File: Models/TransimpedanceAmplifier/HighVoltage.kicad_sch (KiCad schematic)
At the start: 3 parts, among them U11 LM7815, 15V, 5%, U12 LM7915, -15V, 5%

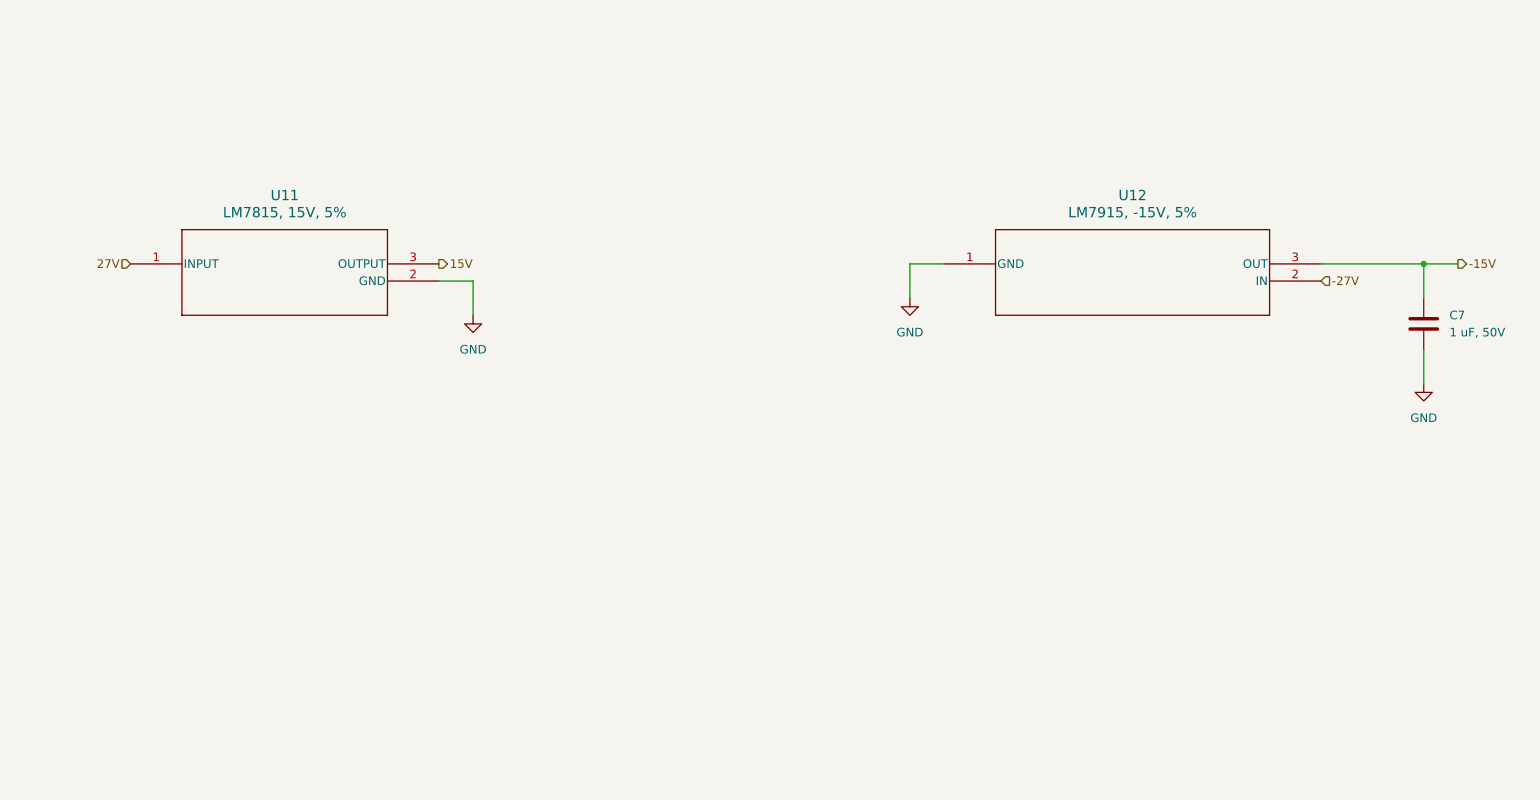
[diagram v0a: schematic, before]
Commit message: Finished the decoupling networks for the power subsystem
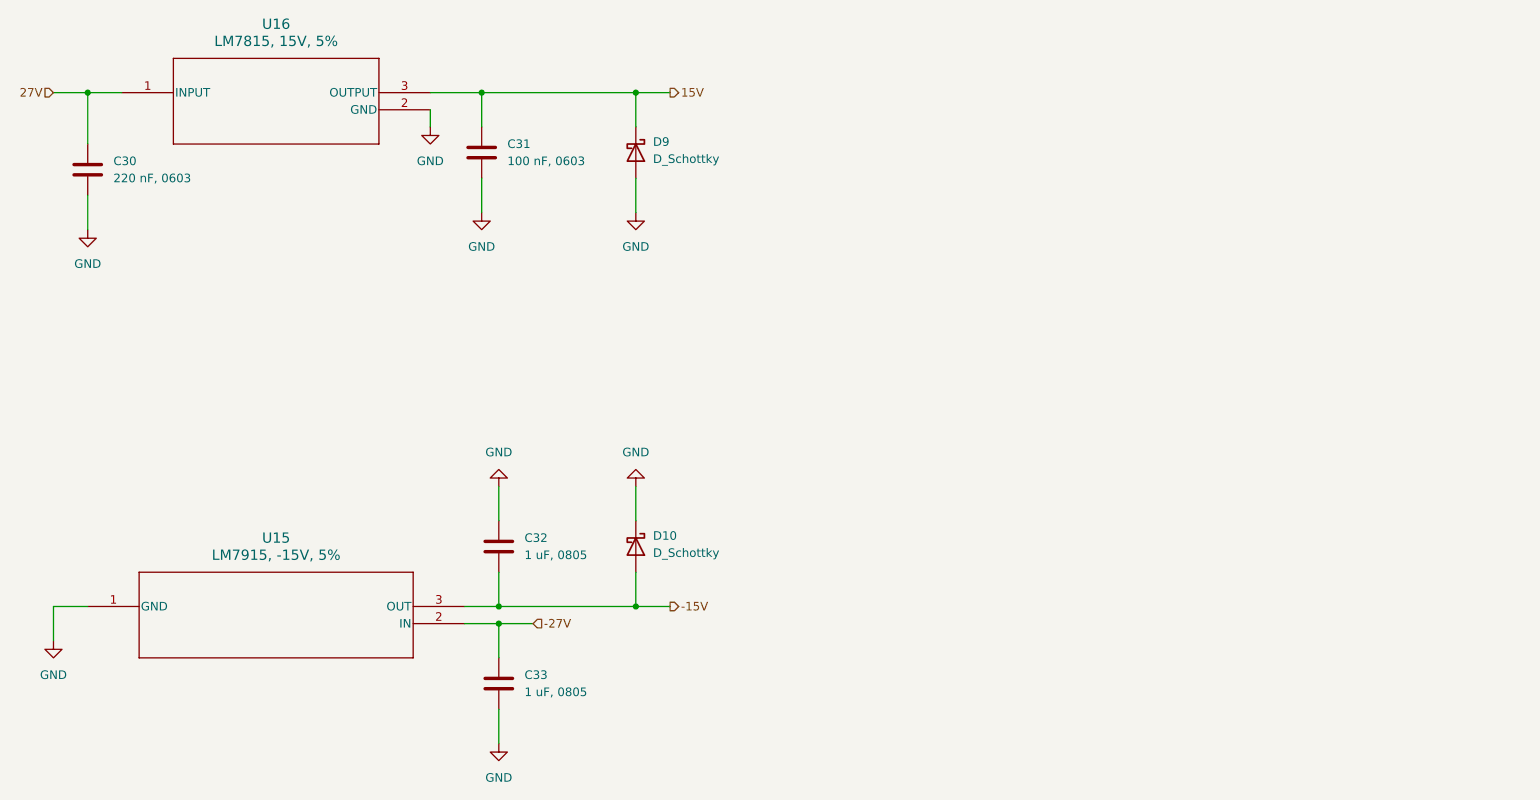
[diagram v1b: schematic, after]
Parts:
- removed C7: 1 uF, 50V, symbol Device:C
- removed U11: LM7815, 15V, 5%, NDE3_TEX, symbol LM78:LM7805CT_NOPB
- removed U12: LM7915, -15V, 5%, T03B_TEX, symbol LM79:LM7905CT
- added C30: 220 nF, 0603, symbol Device:C
- added C31: 100 nF, 0603, symbol Device:C
- added C32, C33: 1 uF, 0805, symbol Device:C
- added D10, D9: D_Schottky, symbol Device:D_Schottky
- added U15: LM7915, -15V, 5%, T03B_TEX, symbol LM79:LM7905CT
- added U16: LM7815, 15V, 5%, NDE3_TEX, symbol LM78:LM7805CT_NOPB
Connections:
- net -15V: now also C32.2, D10.2 (A), U15.3 (OUT)
- net -27V: now also C33.1, U15.2 (IN)
- net 15V: now also C31.1, D9.1 (K), U16.3 (OUTPUT)
- net 27V: now also C30.1, U16.1 (INPUT)
- net GND: now also C30.2, C31.2, C32.1, C33.2, D10.1 (K), D9.2 (A), U15.1 (GND), U16.2 (GND)

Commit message: Finished for today
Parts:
- C30, C31, C32, C33: Purchase Link (none) -> https://www.digikey.com/en/products/detail/murata-electroni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
- D10, D9: Purchase Link (none) -> https://www.digikey.com/en/products/detail/diodes-incorpora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
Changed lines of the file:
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@@
+			)
+		)
+		(property "Purchase Link" "https://www.digikey.com/en/products/detail/murata-electronics/GRM188R71H224KAC4D/5797498"
+			(at 53.34 67.31 0)
+			(effects
+				(font
+					(size 1.27 1.27)
+				)
+				(hide yes)
 			)
 		)
@@
 			)
 		)
+		(property "Purchase Link" "https://www.digikey.com/en/products/detail/murata-electronics/GRM188R72A104KA35D/702549"
+			(at 111.76 64.77 0)
+			(effects
+				(font
+					(size 1.27 1.27)
+				)
+				(hide yes)
+			)
+		)
 		(pin "1"
 		)
@@
 			)
 		)
+		(property "Purchase Link" "https://www.digikey.com/en/products/detail/diodes-incorporated/1N5819HW-7-F/814970"
+			(at 134.62 64.77 90)
+			(effects
+				(font
+					(size 1.27 1.27)
+				)
+				(hide yes)
+			)
+		)
 		(pin "1"
 		)
@@
 			)
 		)
+		(property "Purchase Link" "https://www.digikey.com/en/products/detail/murata-electronics/GRT21BR71H105KE01L/10702345"
+			(at 114.3 143.51 0)
+			(effects
+				(font
+					(size 1.27 1.27)
+				)
+				(hide yes)
+			)
+		)
 		(pin "1"
 		)
@@
 			)
 		)
+		(property "Purchase Link" "https://www.digikey.com/en/products/detail/diodes-incorporated/1N5819HW-7-F/814970"
+			(at 134.62 123.19 90)
+			(effects
+				(font
+					(size 1.27 1.27)
+				)
+				(hide yes)
+			)
+		)
 		(pin "1"
 		)
@@
 			(at 114.3 123.19 0)
 			(effects
+				(font
+					(size 1.27 1.27)
+				)
+				(hide yes)
+			)
+		)
+		(property "Purchase Link" "https://www.digikey.com/en/products/detail/murata-electronics/GRT21BR71H105KE01L/10702345"
+			(at 114.3 123.19 0)
+			(effects

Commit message: Save progress
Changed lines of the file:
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@@
 	)
 	(symbol
+		(lib_name "D_Schottky_1")
 		(lib_id "Device:D_Schottky")
 		(at 134.62 64.77 270)

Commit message: Save progress
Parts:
- U15: footprint T03B_TEX -> (none)
- U16: footprint NDE3_TEX -> (none)
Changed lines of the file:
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@@
 			)
 		)
-		(property "Footprint" "T03B_TEX"
+		(property "Footprint" ""
 			(at 53.34 132.08 0)
 			(effects
@@
 			)
 		)
-		(property "Footprint" "NDE3_TEX"
+		(property "Footprint" ""
 			(at 58.42 55.88 0)
 			(effects

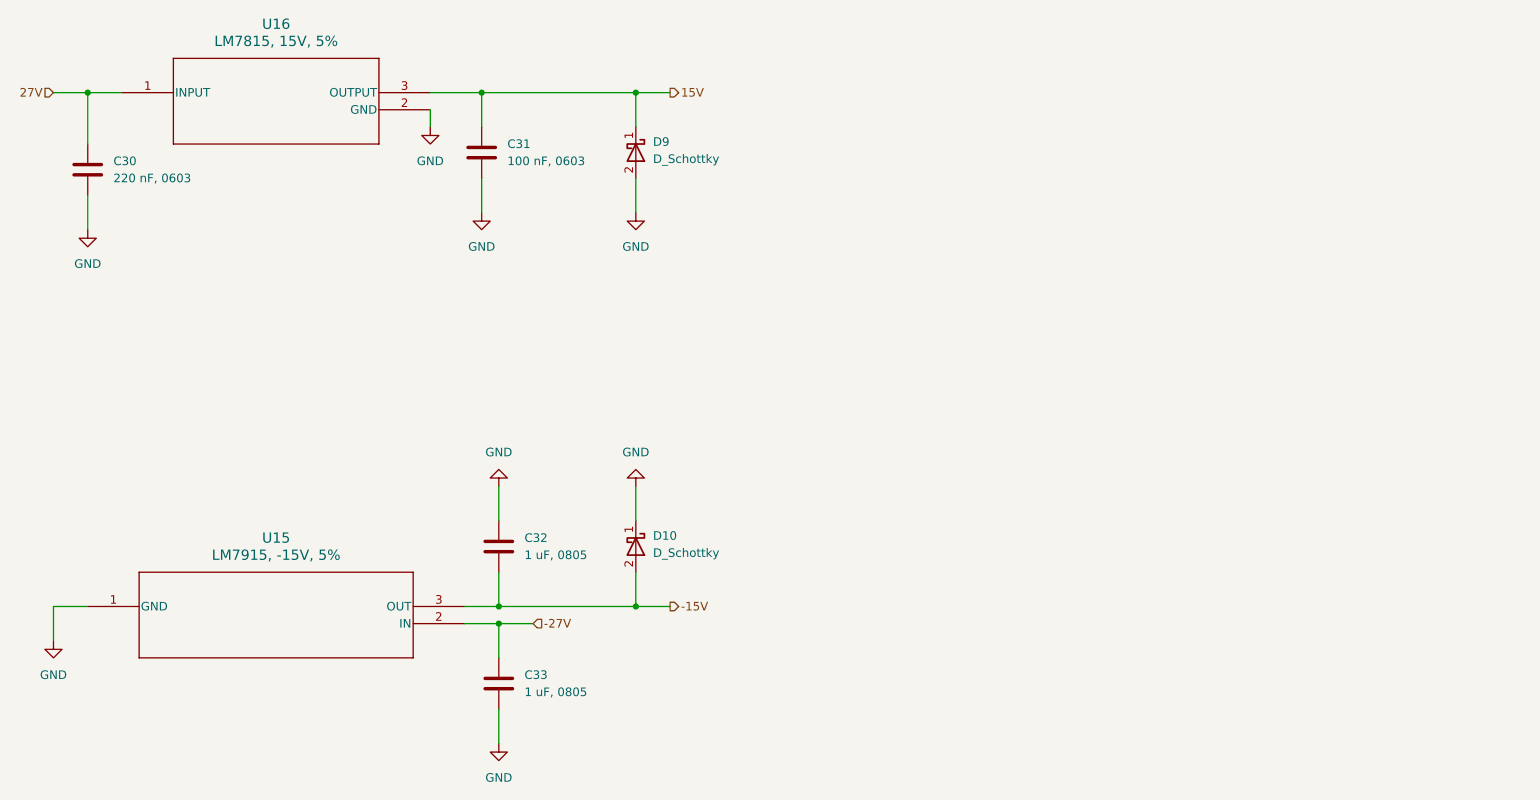
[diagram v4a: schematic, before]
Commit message: Overhauled all of the annotations
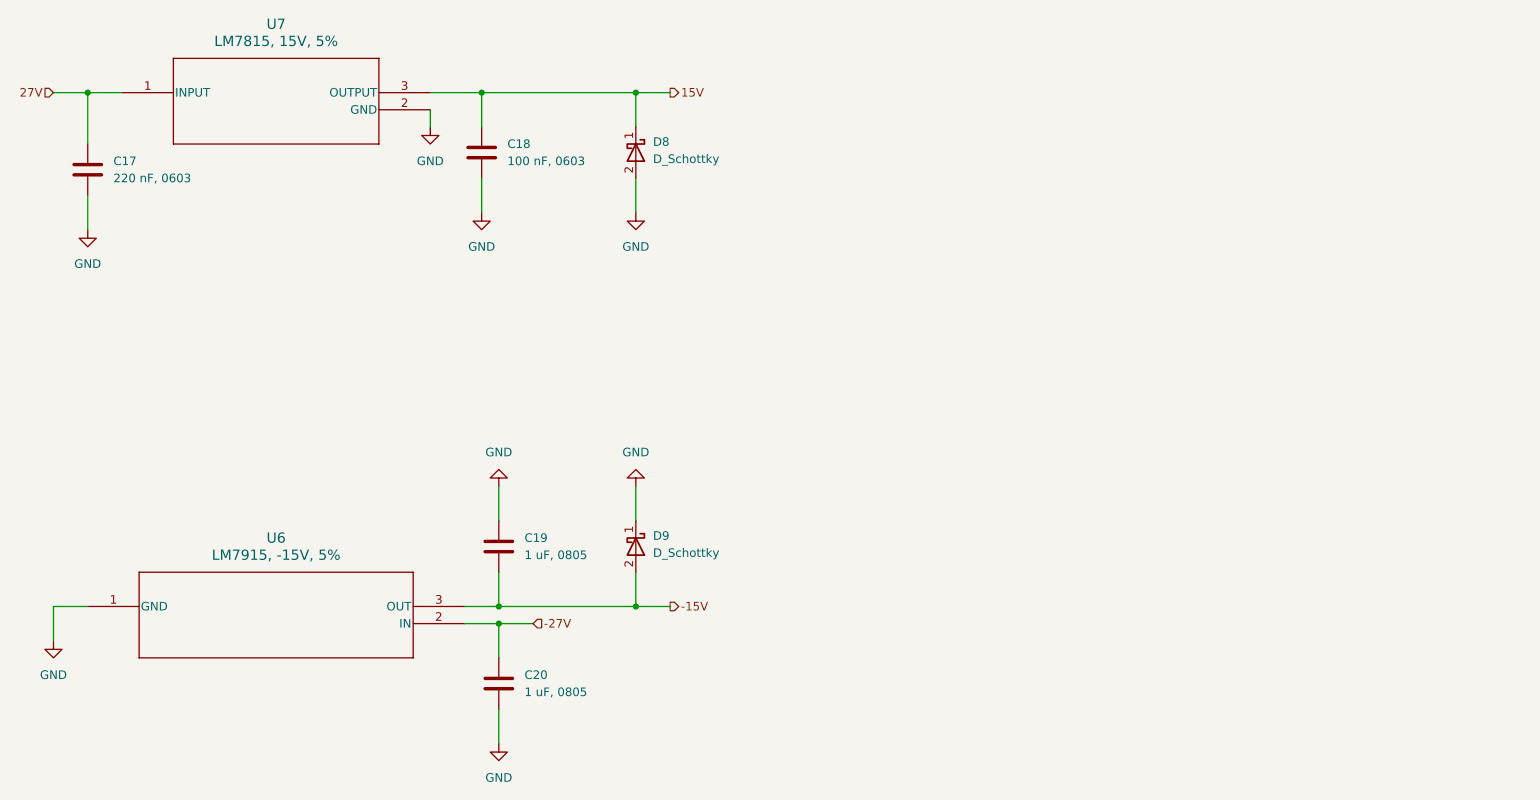
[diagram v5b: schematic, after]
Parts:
- renumbered C30 to C17, C31 to C18, C32 to C19, C33 to C20, D9 to D8, D10 to D9, U15 to U6, U16 to U7
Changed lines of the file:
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@@
 		(dnp no)
 		(fields_autoplaced yes)
-		(property "Reference" "C30"
+		(property "Reference" "C17"
 			(at 57.15 66.0399 0)
 			(effects
@@
 			(project "TransimpedanceAmplifier"
 				(path "/ec9f2ae3-e40d-40eb-9760-2b611ee8efd1/d0ece2d4-5b22-4822-ad0c-e2361683ec3d/79f44061-ff24-463c-a518-31179173364f"
-					(reference "C30")
+					(reference "C17")
 					(unit 1)
 				)
@@
 		(dnp no)
 		(fields_autoplaced yes)
-		(property "Reference" "U15"
+		(property "Reference" "U6"
 			(at 81.28 121.92 0)
 			(effects
@@
 			(project "TransimpedanceAmplifier"
 				(path "/ec9f2ae3-e40d-40eb-9760-2b611ee8efd1/d0ece2d4-5b22-4822-ad0c-e2361683ec3d/79f44061-ff24-463c-a518-31179173364f"
-					(reference "U15")
+					(reference "U6")
 					(unit 1)
 				)
@@
 		(dnp no)
 		(fields_autoplaced yes)
-		(property "Reference" "#PWR040"
+		(property "Reference" "#PWR024"
 			(at 104.14 67.31 0)
 			(effects
@@
 			(project "TransimpedanceAmplifier"
 				(path "/ec9f2ae3-e40d-40eb-9760-2b611ee8efd1/d0ece2d4-5b22-4822-ad0c-e2361683ec3d/79f44061-ff24-463c-a518-31179173364f"
-					(reference "#PWR040")
+					(reference "#PWR024")
 					(unit 1)
 				)
@@
 		(dnp no)
 		(fields_autoplaced yes)
-		(property "Reference" "#PWR039"
+		(property "Reference" "#PWR023"
 			(at 53.34 82.55 0)
 			(effects
@@
 			(project "TransimpedanceAmplifier"
 				(path "/ec9f2ae3-e40d-40eb-9760-2b611ee8efd1/d0ece2d4-5b22-4822-ad0c-e2361683ec3d/79f44061-ff24-463c-a518-31179173364f"
-					(reference "#PWR039")
+					(reference "#PWR023")
 					(unit 1)
 				)
@@
 		(dnp no)
 		(fields_autoplaced yes)
-		(property "Reference" "#PWR045"
+		(property "Reference" "#PWR029"
 			(at 134.62 107.95 0)
 			(effects
@@
 			(project "TransimpedanceAmplifier"
 				(path "/ec9f2ae3-e40d-40eb-9760-2b611ee8efd1/d0ece2d4-5b22-4822-ad0c-e2361683ec3d/79f44061-ff24-463c-a518-31179173364f"
-					(reference "#PWR045")
+					(reference "#PWR029")
 					(unit 1)
 				)
@@
 		(dnp no)
 		(fields_autoplaced yes)
-		(property "Reference" "#PWR041"
+		(property "Reference" "#PWR025"
 			(at 111.76 80.01 0)
 			(effects
@@
 			(project "TransimpedanceAmplifier"
 				(path "/ec9f2ae3-e40d-40eb-9760-2b611ee8efd1/d0ece2d4-5b22-4822-ad0c-e2361683ec3d/79f44061-ff24-463c-a518-31179173364f"
-					(reference "#PWR041")
+					(reference "#PWR025")
 					(unit 1)
 				)
@@
 		(dnp no)
 		(fields_autoplaced yes)
-		(property "Reference" "#PWR044"
+		(property "Reference" "#PWR028"
 			(at 134.62 80.01 0)
 			(effects
@@
 			(project "TransimpedanceAmplifier"
 				(path "/ec9f2ae3-e40d-40eb-9760-2b611ee8efd1/d0ece2d4-5b22-4822-ad0c-e2361683ec3d/79f44061-ff24-463c-a518-31179173364f"
-					(reference "#PWR044")
+					(reference "#PWR028")
 					(unit 1)
 				)
@@
 		(dnp no)
 		(fields_autoplaced yes)
-		(property "Reference" "#PWR038"
+		(property "Reference" "#PWR022"
 			(at 48.26 143.51 0)
 			(effects
@@
 			(project "TransimpedanceAmplifier"
 				(path "/ec9f2ae3-e40d-40eb-9760-2b611ee8efd1/d0ece2d4-5b22-4822-ad0c-e2361683ec3d/79f44061-ff24-463c-a518-31179173364f"
-					(reference "#PWR038")
+					(reference "#PWR022")
 					(unit 1)
 				)
@@
 		(dnp no)
 		(fields_autoplaced yes)
-		(property "Reference" "U16"
+		(property "Reference" "U7"
 			(at 81.28 45.72 0)
 			(effects
@@
 			(project "TransimpedanceAmplifier"
 				(path "/ec9f2ae3-e40d-40eb-9760-2b611ee8efd1/d0ece2d4-5b22-4822-ad0c-e2361683ec3d/79f44061-ff24-463c-a518-31179173364f"
-					(reference "U16")
+					(reference "U7")
 					(unit 1)
 				)
@@
 		(dnp no)
 		(fields_autoplaced yes)
-		(property "Reference" "#PWR042"
+		(property "Reference" "#PWR026"
 			(at 114.3 107.95 0)
 			(effects
@@
 			(project "TransimpedanceAmplifier"
 				(path "/ec9f2ae3-e40d-40eb-9760-2b611ee8efd1/d0ece2d4-5b22-4822-ad0c-e2361683ec3d/79f44061-ff24-463c-a518-31179173364f"
-					(reference "#PWR042")
+					(reference "#PWR026")
 					(unit 1)
 				)
@@
 		(dnp no)
 		(fields_autoplaced yes)
-		(property "Reference" "C31"
+		(property "Reference" "C18"
 			(at 115.57 63.4999 0)
 			(effects
@@
 			(project "TransimpedanceAmplifier"
 				(path "/ec9f2ae3-e40d-40eb-9760-2b611ee8efd1/d0ece2d4-5b22-4822-ad0c-e2361683ec3d/79f44061-ff24-463c-a518-31179173364f"
-					(reference "C31")
+					(reference "C18")
 					(unit 1)
 				)
@@
 		(dnp no)
 		(fields_autoplaced yes)
-		(property "Reference" "D9"
+		(property "Reference" "D8"
 			(at 137.16 63.1824 90)
 			(effects
@@
 			(project "TransimpedanceAmplifier"
 				(path "/ec9f2ae3-e40d-40eb-9760-2b611ee8efd1/d0ece2d4-5b22-4822-ad0c-e2361683ec3d/79f44061-ff24-463c-a518-31179173364f"
-					(reference "D9")
+					(reference "D8")
 					(unit 1)
 				)
@@
 		(dnp no)
 		(fields_autoplaced yes)
-		(property "Reference" "C33"
+		(property "Reference" "C20"
 			(at 118.11 142.2399 0)
 			(effects
@@
 			(project "TransimpedanceAmplifier"
 				(path "/ec9f2ae3-e40d-40eb-9760-2b611ee8efd1/d0ece2d4-5b22-4822-ad0c-e2361683ec3d/79f44061-ff24-463c-a518-31179173364f"
-					(reference "C33")
+					(reference "C20")
 					(unit 1)
 				)
@@
 		(dnp no)
 		(fields_autoplaced yes)
-		(property "Reference" "D10"
+		(property "Reference" "D9"
 			(at 137.16 121.6024 90)
 			(effects
@@
 			(project "TransimpedanceAmplifier"
 				(path "/ec9f2ae3-e40d-40eb-9760-2b611ee8efd1/d0ece2d4-5b22-4822-ad0c-e2361683ec3d/79f44061-ff24-463c-a518-31179173364f"
-					(reference "D10")
+					(reference "D9")
 					(unit 1)
 				)
@@
 		(dnp no)
 		(fields_autoplaced yes)
-		(property "Reference" "C32"
+		(property "Reference" "C19"
 			(at 118.11 121.9199 0)
 			(effects
@@
 			(project "TransimpedanceAmplifier"
 				(path "/ec9f2ae3-e40d-40eb-9760-2b611ee8efd1/d0ece2d4-5b22-4822-ad0c-e2361683ec3d/79f44061-ff24-463c-a518-31179173364f"
-					(reference "C32")
+					(reference "C19")
 					(unit 1)
 				)
@@
 		(dnp no)
 		(fields_autoplaced yes)
-		(property "Reference" "#PWR043"
+		(property "Reference" "#PWR027"
 			(at 114.3 158.75 0)
 			(effects
@@
 			(project "TransimpedanceAmplifier"
 				(path "/ec9f2ae3-e40d-40eb-9760-2b611ee8efd1/d0ece2d4-5b22-4822-ad0c-e2361683ec3d/79f44061-ff24-463c-a518-31179173364f"
-					(reference "#PWR043")
-					(unit 1)
-				)
+					(reference "#PWR027")
+					(unit 1)
+				)
